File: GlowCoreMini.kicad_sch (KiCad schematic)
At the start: 34 parts, among them J2 DC-042C-Z-2.5-A, J3 Conn_02x06_Counter_Clockwise, J4 WJ500V-5.08-3P, Q1 SK338P, Q2 MMBT2222A, Q3 MMBT2222A, SW1 TS-1185EC-C-D-B, U1 SN74AHCT32QPWRQ1, U2 ESP32-WROOM-32E (4MB), U3 BL1117-33CX, U4 CP2104

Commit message: updated pcb design (still in dev)
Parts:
- removed C5: 1uF, Capacitor_SMD:C_0603_1608Metric_Pad1.08x0.95mm_HandSolder, symbol Device:1uF 0603
- removed C6: 10uF, Capacitor_SMD:C_0603_1608Metric_Pad1.08x0.95mm_HandSolder, symbol Device:10uF 0603
- removed J3: Conn_02x06_Counter_Clockwise, Connector_PinSocket_2.54mm:PinSocket_2x06_P2.54mm_Vertical, symbol Connector_Generic:Conn_02x06_Counter_Clockwise
- removed J4: WJ500V-5.08-3P, TerminalBlock_Phoenix:TerminalBlock_Phoenix_MKDS-1,5-3-5.08_1x03_P5.08mm_Horizontal, symbol Connector_Generic:WJ500V-5.08-3P
- removed Q1: SK338P, Package_TO_SOT_SMD:SOT-23, symbol Transistor_FET:SK338P
- removed R2: 100K, Resistor_SMD:R_0603_1608Metric_Pad0.98x0.95mm_HandSolder, symbol Device:100K 0603
- removed U4: CP2104, Package_DFN_QFN:QFN-24-1EP_4x4mm_P0.5mm_EP2.6x2.6mm, symbol Interface_USB:CP2104
- added C10: 0.1uF, Capacitor_SMD:C_0603_1608Metric_Pad1.08x0.95mm_HandSolder, symbol Device:0.1uF_0603
- added C6: 4.7uF 6.3V 10%, Capacitor_SMD:C_0603_1608Metric_Pad1.08x0.95mm_HandSolder, symbol Device:C
- added J1: Conn_01x06, Connector_PinSocket_2.54mm:PinSocket_1x06_P2.54mm_Vertical, symbol Connector_Generic:Conn_01x06
- added P1: WJ15EDGRC-3.81-3P, WJ15EDGRC:WJ15EDGRC-3.81-3P, symbol WJ15EDGRC:WJ15EDGRC-3.81-3P
- added U4: CP2102-GMR, CP2102-GMR:CP2102-GMR, symbol CP2102-GMR:CP2102-GMR
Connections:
- net USB-C VBUS is gone; now on net +5V: D1.1 (K)
- net +3V3: now also C10.1, C6.2, J1.3 (Pin_3), U4.6 (VDD), U4.7 (REGIN)
- net +5V: now also J1.1 (Pin_1), P1.1, U4.8 (VBUS)
- net DTR: now also U4.28 (DTR)
- net GND: now also U1.11 (4Y), U1.12 (4A), U1.4 (2A), U1.6 (2Y), U1.8 (3Y), U1.9 (3A), USB1.B1A12 (GND), C10.2, C6.1, J1.2 (Pin_2), P1.3, U4.29 (GND_PAD), U4.3 (GND); no longer USB1.8 (GND)
- net IO13: now also J1.6 (Pin_6)
- net IO25/A1/DAC1: now also J1.5 (Pin_5)
- net IO26/A0/DAC2: now also J1.4 (Pin_4)
- net RTS: now also U4.24 (RTS)
- net RXD0: now also U4.26 (TXD)
- net TXD0: now also U4.25 (RXD)
- net USB-C DATA+: now also U4.4 (D+)
- net USB-C DATA-: now also U4.5 (D-)
- net at R1.2: now also P1.2
- no-connect marks 0 -> 11
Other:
- moved on the sheet: C3, C4, C7, MK1, R4, U3

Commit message: update design
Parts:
- added C11, C12, C5: 220uF 10V, Capacitor_SMD:CP_Elec_6.3x5.4, symbol Device:220uF 10V 6.3x5.4mm
- added F1: BSMD1812-300-16V, Fuse:Fuse_1812_4532Metric_Pad1.30x3.40mm_HandSolder, symbol Device:Fuse
- added F2: JK16-800, JK16-800:JK16-800, symbol JK16-800:JK16-800
- C2: value 220uF 10V 6.3x5.4mm -> 220uF 10V
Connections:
- net +5V: now also C11.1, C12.1, C5.1, F2.1; no longer J2.3
- net GND: now also C11.2, C12.2, C5.2
- net IO13: no longer U2.16 (IO13)
- net at USB1.A4B9 (VBUS), USB1.B4A9 (VBUS): now also F1.1; no longer D1.2 (A)
- net IO12 renamed IO12/MISO
- net IO18/MOSI renamed IO18
- net IO19/MISO renamed IO19
- new net: F2.2, J2.3
- new net: D1.2 (A), F1.2
- new net IO13/MOSI: U2.16 (IO13)
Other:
- moved on the sheet: C2, D1, J2

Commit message: work on updated pcb design
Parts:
- removed C11, C12: 220uF 10V, Capacitor_SMD:CP_Elec_6.3x5.4, symbol Device:220uF 10V 6.3x5.4mm
- removed F1: BSMD1812-300-16V, Fuse:Fuse_1812_4532Metric_Pad1.30x3.40mm_HandSolder, symbol Device:Fuse
- removed F2: JK16-800, JK16-800:JK16-800, symbol JK16-800:JK16-800
- removed R4: 100K, Resistor_SMD:R_0603_1608Metric_Pad0.98x0.95mm_HandSolder, symbol Device:100K 0603
- removed Status_LED1: SolderJumper_2_Open, Jumper:SolderJumper-2_P1.3mm_Open_Pad1.0x1.5mm, symbol Jumper:SolderJumper_2_Open
- added R2: 100K, Resistor_SMD:R_0603_1608Metric_Pad0.98x0.95mm_HandSolder, symbol Device:100K 0603
- D1: value B340A-13-F -> SS54; 150+ €0.1159 -> (none); 5+ €0.1491 -> (none); 50+ €0.1307 -> (none); LCSC Part # C85098 -> (none); LCSC link https://lcsc.com/product-detail/Schottky-Barrier-Diodes-SBD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 -> (none); Manufacturer Diodes Incorporated -> Shandong Jingdao Microelectronics; Mfr. Part # B340A-13-F -> (none)
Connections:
- net +5V: now also J2.3
- net GND: now also R2.2
- net IO13: now also R7.1
- net IO32/SD: now also MK1.7 (SD), R2.1
- net at USB1.A4B9 (VBUS), USB1.B4A9 (VBUS): now also D1.2 (A)
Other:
- moved on the sheet: D1, D2, R7, USB1

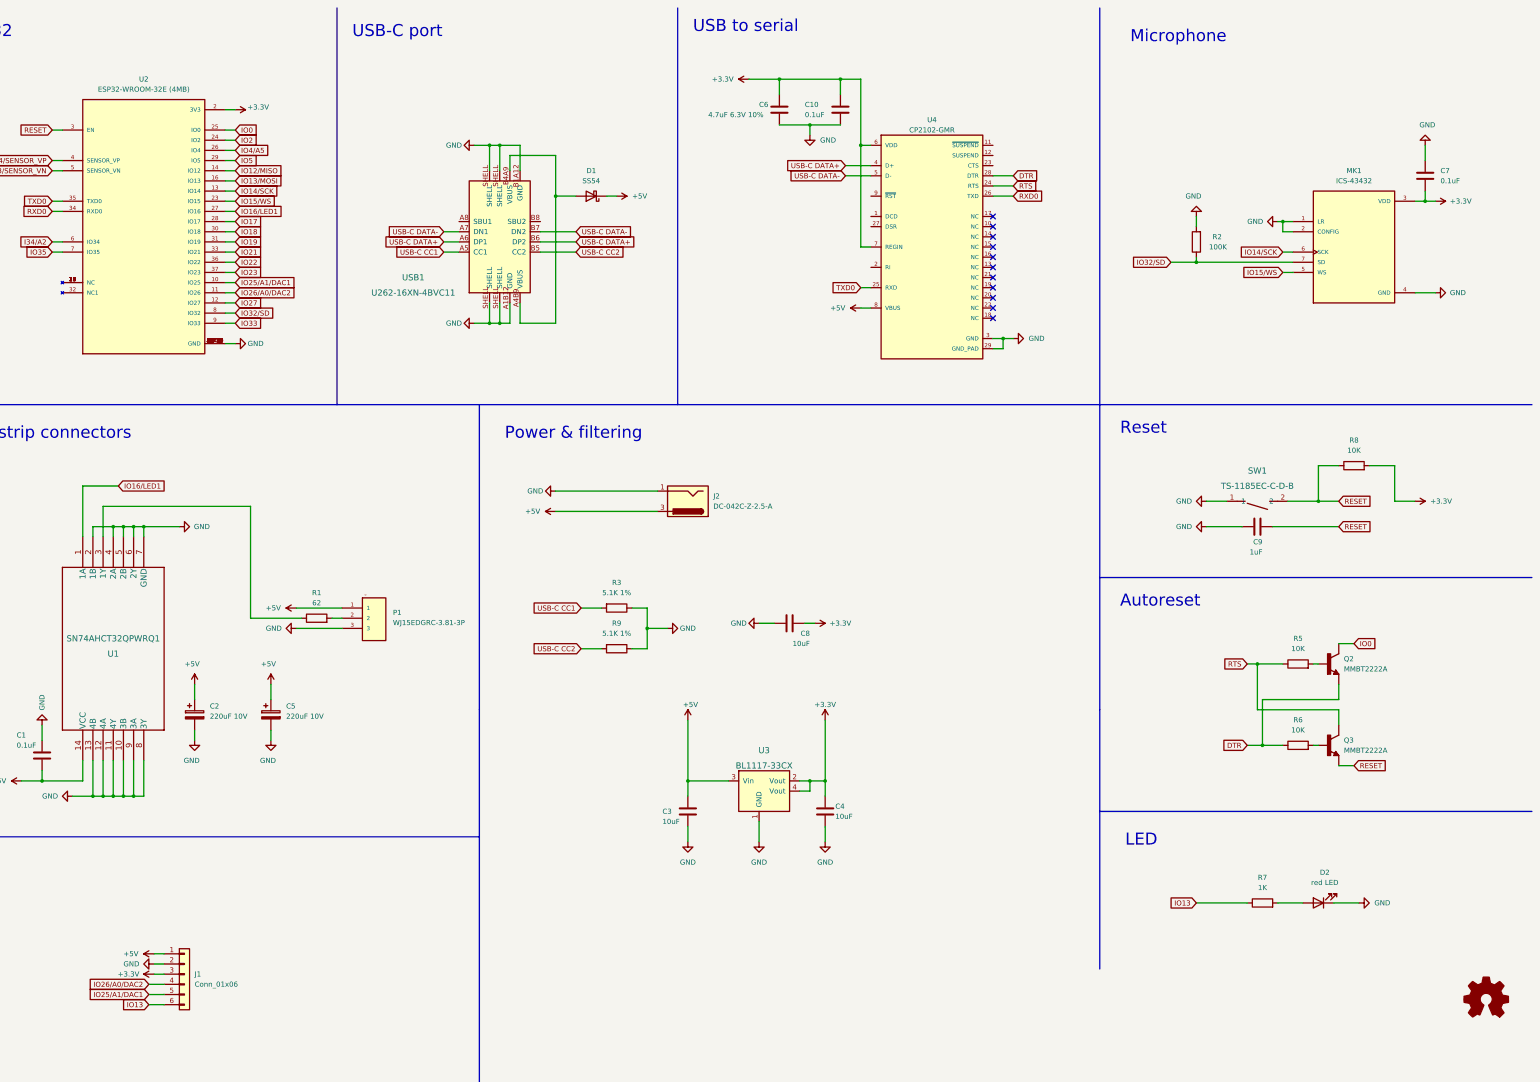
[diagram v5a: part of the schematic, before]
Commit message: added GlowCore Mini dev board v1.0 beta 1
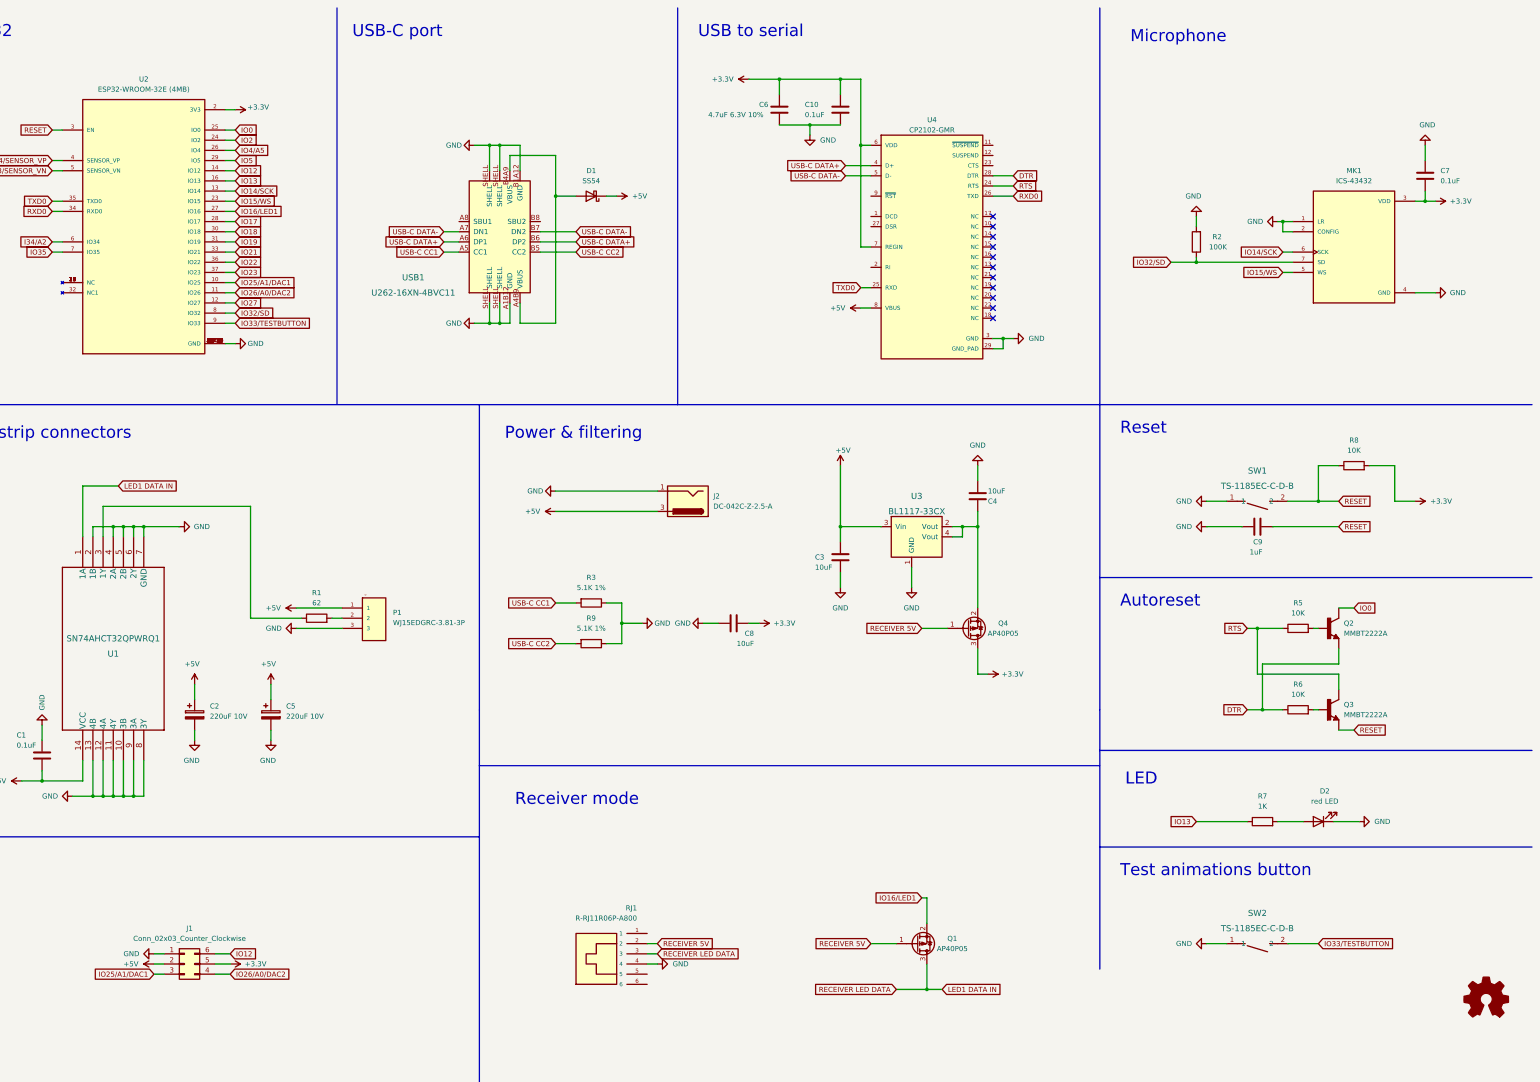
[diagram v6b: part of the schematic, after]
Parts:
- removed J1: Conn_01x06, Connector_PinSocket_2.54mm:PinSocket_1x06_P2.54mm_Vertical, symbol Connector_Generic:Conn_01x06
- added J1: Conn_02x03_Counter_Clockwise, Connector_PinSocket_2.54mm:PinSocket_2x03_P2.54mm_Vertical, symbol Connector_Generic:Conn_02x03_Counter_Clockwise
- added Q1, Q4: AP40P05, Package_TO_SOT_SMD:SOT-23, symbol Transistor_FET:SK338P
- added RJ1: R-RJ11R06P-A800, R-RJ11R06P-A800:R-RJ11R06P-A800, symbol R-RJ11R06P-A800:PCB-6P6C-90
- added SW2: TS-1185EC-C-D-B, TS-1185EC-C-D-B:TS-1185EC-C-D-B, symbol TS-1185EC-C-D-B:TS-1185EC-C-D-B
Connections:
- net IO13/MOSI is gone; now on net IO13: U2.16 (IO13)
- net +3V3: now also J1.5 (Pin_5), Q4.3 (D); no longer C4.2, U3.2 (Vout), U3.4 (Vout)
- net +5V: now also J1.2 (Pin_2)
- net GND: now also J1.1 (Pin_1), RJ1.4, SW2.1
- net IO16/LED1: now also Q1.2 (S); no longer U1.1 (1A)
- net IO25/A1/DAC1: now also J1.3 (Pin_3)
- net IO26/A0/DAC2: now also J1.4 (Pin_4)
- net IO12/MISO renamed IO12
- net IO12: now also J1.6 (Pin_6)
- net IO33 renamed IO33/TESTBUTTON
- net IO33/TESTBUTTON: now also SW2.2
- new net: C4.2, Q4.2 (S), U3.2 (Vout), U3.4 (Vout)
- new net LED1 DATA IN: Q1.3 (D), RJ1.3, U1.1 (1A)
- new net RECEIVER 5V: Q1.1 (G), Q4.1 (G), RJ1.2
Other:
- note added: "Receiver mode"
- note added: "Test animations button"
- moved on the sheet: C3, C4, C8, D2, Q2, Q3, R3, R5, R6, R7, R9, U3

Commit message: add warning info
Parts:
- removed C5: 220uF 10V, Capacitor_SMD:CP_Elec_6.3x5.4, symbol Device:220uF 10V 6.3x5.4mm
- removed C9: 1uF, Capacitor_SMD:C_0603_1608Metric_Pad1.08x0.95mm_HandSolder, symbol Device:1uF 0603
- removed D2: red LED, LED_SMD:LED_0603_1608Metric_Pad1.05x0.95mm_HandSolder, symbol Device:red LED 0603
- removed J2: DC-042C-Z-2.5-A, DC-042C-Z-2:DC-IN-TH_DC-042C-Z-2.5-A, symbol Connector:DC-042C-Z-2.5-A
- removed MK1: ICS-43432, ICS-43432:MIC_ICS-43432, symbol ICS-43432:ICS-43432
- removed Q1, Q4: AP40P05, Package_TO_SOT_SMD:SOT-23, symbol Transistor_FET:SK338P
- removed Q2, Q3: MMBT2222A, Package_TO_SOT_SMD:SOT-23, symbol MMBT2222A:MMBT2222A
- removed R2: 100K, Resistor_SMD:R_0603_1608Metric_Pad0.98x0.95mm_HandSolder, symbol Device:100K 0603
- removed R7: 1K, Resistor_SMD:R_0603_1608Metric_Pad0.98x0.95mm_HandSolder, symbol Device:1K_0603
- removed R8: 10K, Resistor_SMD:R_0603_1608Metric_Pad0.98x0.95mm_HandSolder, symbol Device:10K 0603
- removed U3: BL1117-33CX, Package_TO_SOT_SMD:SOT-223, symbol BL1117-33CX:BL1117-33CX
- added C5: 10uF, Capacitor_SMD:C_0603_1608Metric_Pad1.08x0.95mm_HandSolder, symbol Device:10uF 0603
- added C9: 1nF, Capacitor_SMD:C_0603_1608Metric_Pad1.08x0.95mm_HandSolder, symbol Device:10uF 0603
- added LED1: (no value), symbol LCSC:WS2812B-2020
- added R2, R4: 220, Resistor_SMD:R_0603_1608Metric_Pad0.98x0.95mm_HandSolder, symbol Device:10K 0603
- added SW3: TS-1185EC-C-D-B, TS-1185EC-C-D-B:TS-1185EC-C-D-B, symbol TS-1185EC-C-D-B:TS-1185EC-C-D-B
- added U3: (no value), symbol LCSC:KF350-3_5-2P
- added U5: BL1117-33CX, Package_TO_SOT_SMD:SOT-223, symbol BL1117-33CX:BL1117-33CX
- added U6: UMH3N, footprint:SC-70-6_L2.2-W1.3-P0.65-LS2.1-BR, symbol LCSC:UMH3N
- added U7: GMA4030H11-F26, GMA4030H11-F26:GMA4030H11-F26, symbol GMA4030H11-F26:GMA4030H11-F26
- C8: value 10uF -> 1nF
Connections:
- net +3V3: now also C3.2, R5.2, R6.2, C5.2, U5.2 (Vout), U5.4 (Vout), U7.1 (VDD); no longer C8.1
- net +5V: now also C4.2, U3.2, U5.3 (Vin); no longer C3.2
- net DTR: now also U6.2 (B), U6.4 (E); no longer R6.1
- net GND: now also C5.1, C9.2, SW3.1, U3.1, U5.1 (GND), U7.5 (GND), U7.6 (GND), U7.7 (GND), U7.8 (GND)
- net IO0: now also R6.1, C9.1, R4.2, U6.3 (C)
- net IO13: now also LED1.3 (DI)
- net IO14/SCK: now also U7.3 (CLOCK)
- net IO15/WS: now also U7.2 (SELECT)
- net IO32/SD: now also U7.4 (DATA)
- net IO33/TESTBUTTON: now also SW3.2; no longer SW2.2
- net RESET: now also C8.1, R5.1, R2.2, U6.6 (C); no longer SW1.2
- net RTS: now also U6.1 (E), U6.5 (B); no longer R5.1
- new net: R4.1, SW2.2
- new net: R2.1, SW1.2
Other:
- note added: "Auto program DTR RTS --> EN IO0 1 1 1 1 0 0 1 1 1 0 0 1 0 1 1 0"
- moved on the sheet: R3, R9
